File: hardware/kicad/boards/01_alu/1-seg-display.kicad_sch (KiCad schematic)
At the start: 11 parts, among them U233 74LS377, U234 HDSP-A153

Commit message: chore: annotated and locked design-in
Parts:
- renumbered C233 to C238, U233 to U238, U234 to U239

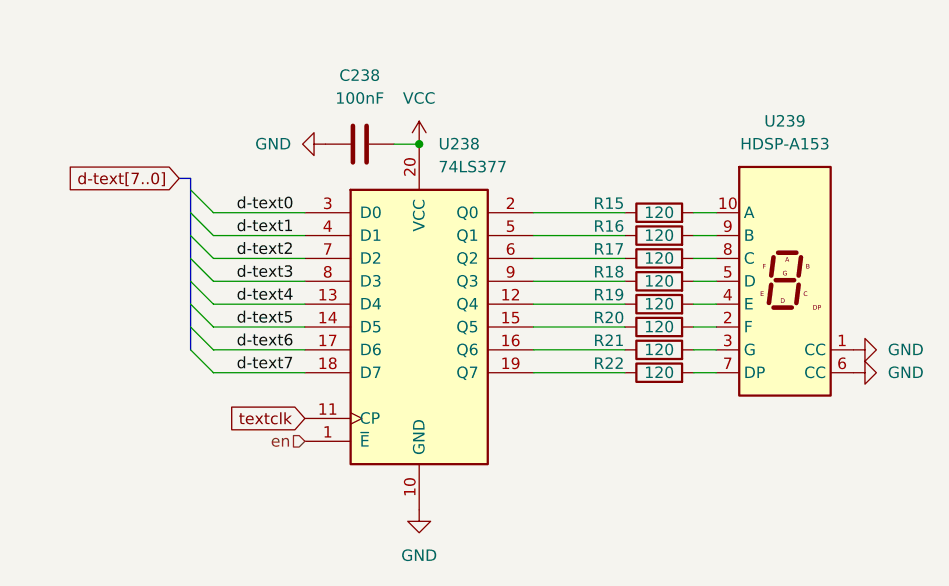
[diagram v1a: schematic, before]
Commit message: chore: refactored display logic and cleanup alu design
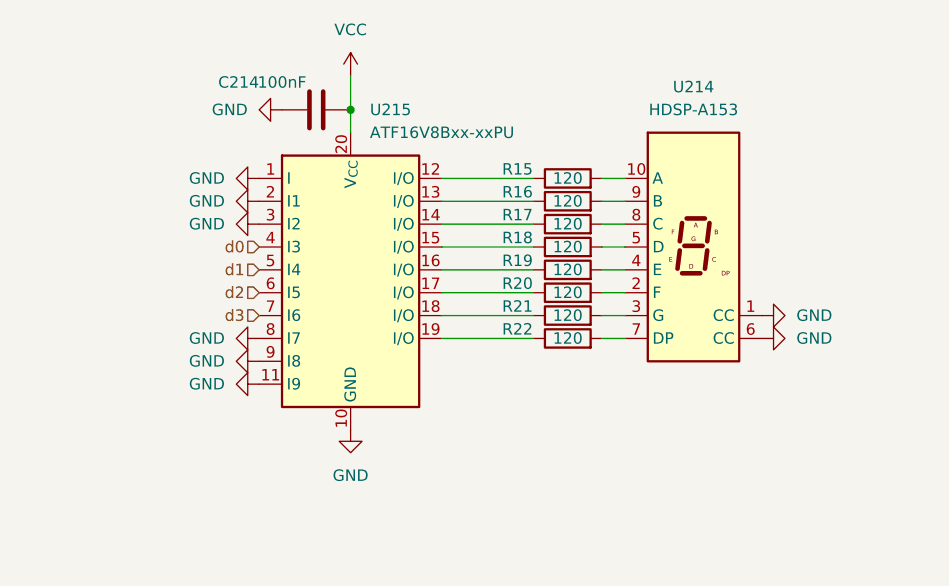
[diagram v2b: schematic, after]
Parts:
- removed C238: 100nF, Capacitor_SMD:C_0805_2012Metric, symbol Device:C
- removed U238: 74LS377, Package_SO:SOIC-20W_7.5x12.8mm_P1.27mm, symbol 74xx:74LS377
- removed U239: HDSP-A153, Display_7Segment:HDSP-A151, symbol Display_Character:HDSP-A153
- added C214: 100nF, Capacitor_SMD:C_0603_1608Metric, symbol Device:C
- added U214: HDSP-A153, Display_7Segment:HDSP-A151, symbol Display_Character:HDSP-A153
- added U215: ATF16V8Bxx-xxPU, Package_SO:SOIC-20W_7.5x12.8mm_P1.27mm, symbol Logic_Programmable:ATF16V8Bxx-xxPU
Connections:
- net GND: now also C214.1, U214.1 (CC), U214.6 (CC), U215.1 (I), U215.10 (GND), U215.11 (I9), U215.2 (I1), U215.3 (I2), U215.8 (I7), U215.9 (I8)
- net VCC: now also C214.2, U215.20 (V_{CC})
- net at R19.1: now also U215.16 (I/O)
- net at R19.2: now also U214.4 (E)
- net at R16.1: now also U215.13 (I/O)
- net at R16.2: now also U214.9 (B)
- net at R20.1: now also U215.17 (I/O)
- net at R21.1: now also U215.18 (I/O)
- net at R22.1: now also U215.19 (I/O)
- net at R15.1: now also U215.12 (I/O)
- net at R17.1: now also U215.14 (I/O)
- net at R18.1: now also U215.15 (I/O)
- net at R15.2: now also U214.10 (A)
- net at R20.2: now also U214.2 (F)
- net at R21.2: now also U214.3 (G)
- net at R18.2: now also U214.5 (D)
- net at R22.2: now also U214.7 (DP)
- net at R17.2: now also U214.8 (C)
- new net d0: U215.4 (I3)
- new net d1: U215.5 (I4)
- new net d2: U215.6 (I5)
- new net d3: U215.7 (I6)

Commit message: arch: redesigned segment displays with ATF16V8B
Clearly a "bloated" choice, but I need the display to be as robust and stable as possible for debugging purposes. While time multiplexing works well, the hardware for multiplexing for 32b x3 + 1 out is much more complicated than a flat system that takes a nibble and outputs to a segment display
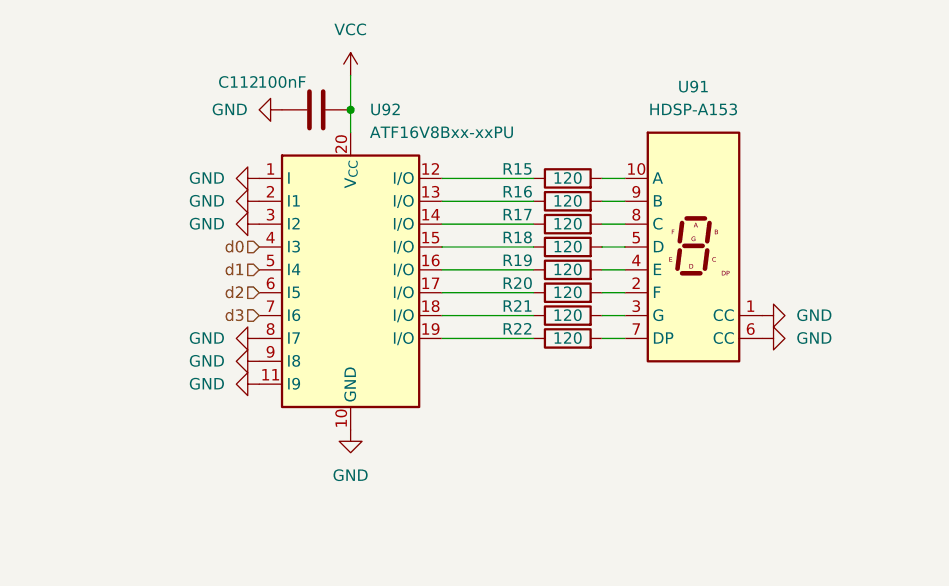
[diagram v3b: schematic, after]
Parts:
- renumbered C214 to C112, U214 to U91, U215 to U92
